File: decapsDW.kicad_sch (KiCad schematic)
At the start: 5 parts

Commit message: adding connectors for display and pi power, pin headers
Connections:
- net DW_VDD1 renamed 3V3_RADAR
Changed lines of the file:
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@@
-    (stroke (width 0) (type default))
-  )
-  (wire (pts (xy 22.86 43.18) (xy 22.86 27.94))
     (stroke (width 0) (type default))
   )
@@
     (stroke (width 0) (type default))
   )
-  (wire (pts (xy 22.86 43.18) (xy 29.21 43.18))
+  (wire (pts (xy 26.67 36.83) (xy 26.67 43.18))
+    (stroke (width 0) (type default))
+  )
+  (wire (pts (xy 26.67 43.18) (xy 29.21 43.18))
     (stroke (width 0) (type default))
   )
@@
     )
   )
-  (global_label "VOUT1" (shape bidirectional) (at 22.86 43.18 180) (fields_autoplaced)
-    (effects (font (size 1.27 1.27)) (justify right))
-    (property "Intersheetrefs" "${INTERSHEET_REFS}" (at 12.8368 43.18 0)
-      (effects (font (size 1.27 1.27)) (justify right) hide)
-    )
-  )
   (global_label "DW_VDD2B" (shape bidirectional) (at 62.23 82.55 0) (fields_autoplaced)
     (effects (font (size 1.27 1.27)) (justify left))
@@
     )
   )
+  (global_label "3V3_RADAR" (shape bidirectional) (at 26.67 43.18 180) (fields_autoplaced)
+    (effects (font (size 1.27 1.27)) (justify right))
+    (property "Intersheetrefs" "${INTERSHEET_REFS}" (at 12.1111 43.18 0)
+      (effects (font (size 1.27 1.27)) (justify right) hide)
+    )
+  )
   (global_label "DW_VDD1" (shape bidirectional) (at 60.96 43.18 0) (fields_autoplaced)
     (effects (font (size 1.27 1.27)) (justify left))
@@
     )
   )
-  (symbol (lib_id "power:PWR_FLAG") (at 22.86 27.94 0) (unit 1)
-    (in_bom yes) (on_board yes) (dnp no) (fields_autoplaced)
-    (property "Reference" "#FLG02" (at 22.86 26.035 0)
-      (effects (font (size 1.27 1.27)) hide)
-    )
-    (property "Value" "PWR_FLAG" (at 22.86 22.86 0)
-      (effects (font (size 1.27 1.27)))
-    )
-    (property "Footprint" "" (at 22.86 27.94 0)
-      (effects (font (size 1.27 1.27)) hide)
-    )
-    (property "Datasheet" "~" (at 22.86 27.94 0)
-      (effects (font (size 1.27 1.27)) hide)
-    )
+  (symbol (lib_id "power:PWR_FLAG") (at 26.67 36.83 0) (unit 1)
+    (in_bom yes) (on_board yes) (dnp no) (fields_autoplaced)
+    (property "Reference" "#FLG02" (at 26.67 34.925 0)
+      (effects (font (size 1.27 1.27)) hide)
+    )
+    (property "Value" "PWR_FLAG" (at 26.67 31.75 0)
+      (effects (font (size 1.27 1.27)))
+    )
+    (property "Footprint" "" (at 26.67 36.83 0)
+      (effects (font (size 1.27 1.27)) hide)
+    )
+    (property "Datasheet" "~" (at 26.67 36.83 0)
+      (effects (font (size 1.27 1.27)) hide)
+    )

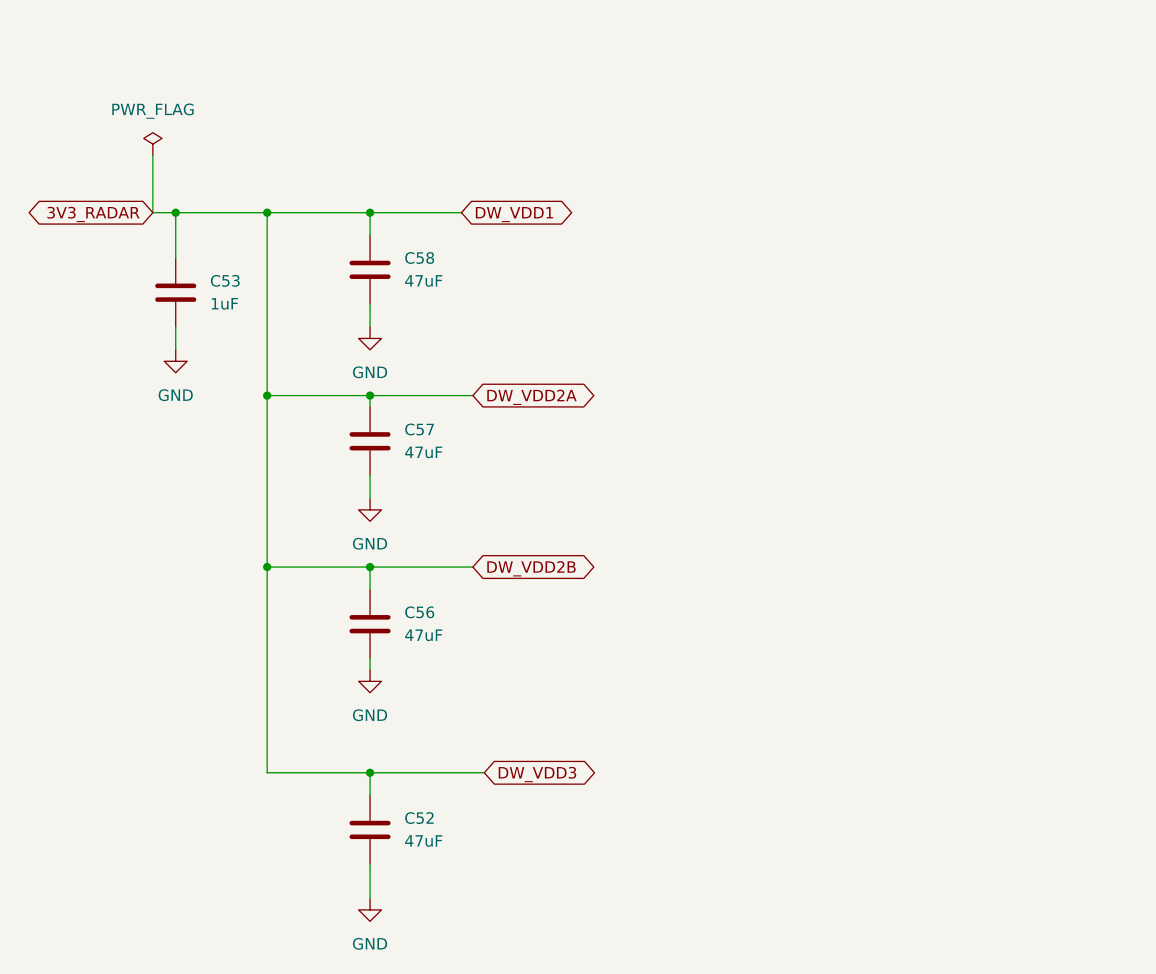
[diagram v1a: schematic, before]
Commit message: changing decoup cap sizes for rf ic
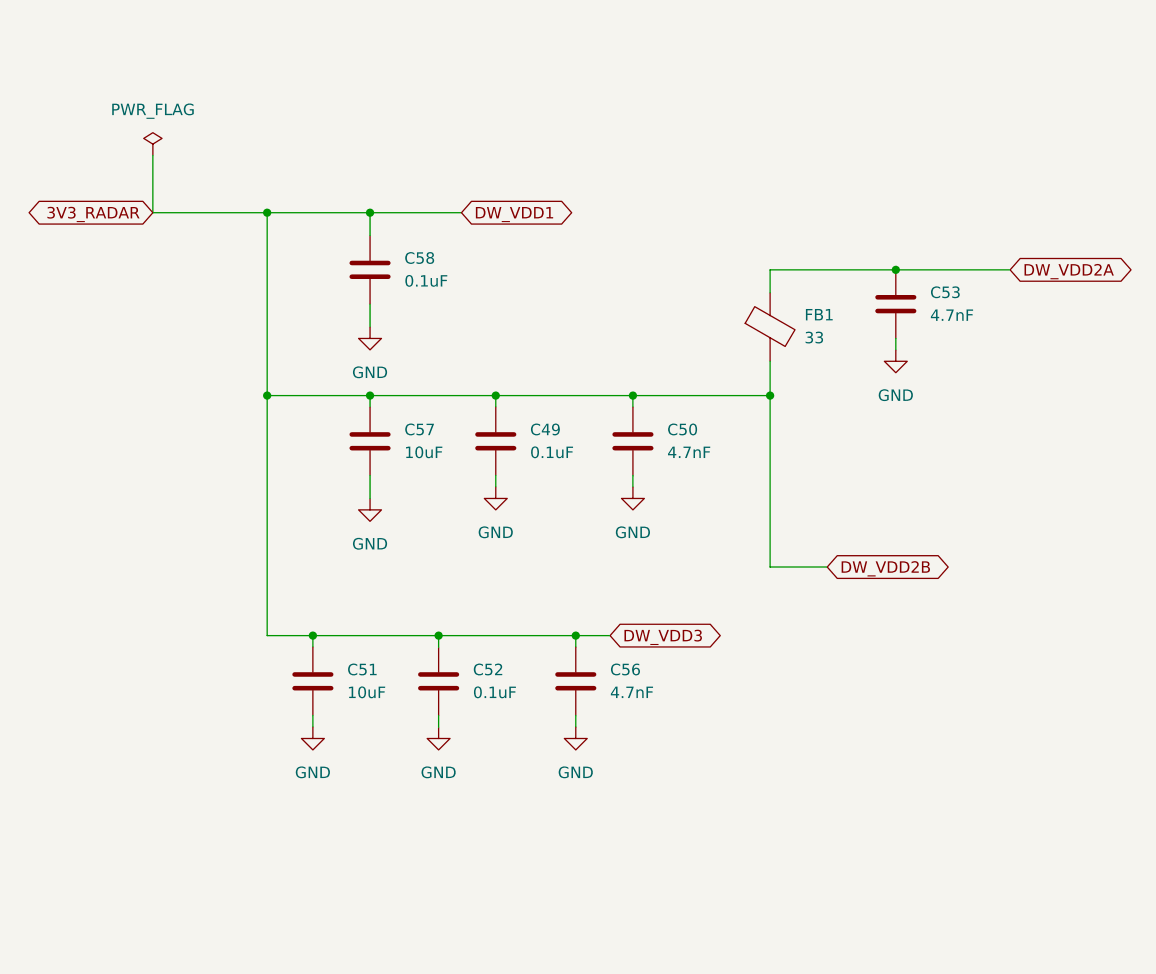
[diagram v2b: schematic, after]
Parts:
- added C49: 0.1uF, Capacitor_SMD:C_0402_1005Metric, symbol Device:C
- added C50: 4.7nF, Capacitor_SMD:C_0402_1005Metric, symbol Device:C
- added C51: 10uF, Capacitor_SMD:C_0402_1005Metric, symbol Device:C
- added FB1: 33, Capacitor_SMD:C_0402_1005Metric, symbol Device:FerriteBead
- C52, C58: value 47uF -> 0.1uF; footprint Capacitor_SMD:C_0603_1608Metric -> Capacitor_SMD:C_0402_1005Metric
- C53: value 1uF -> 4.7nF; footprint Capacitor_SMD:C_0603_1608Metric -> Capacitor_SMD:C_0402_1005Metric
- C56: value 47uF -> 4.7nF; footprint Capacitor_SMD:C_0603_1608Metric -> Capacitor_SMD:C_0402_1005Metric
- C57: value 47uF -> 10uF; footprint Capacitor_SMD:C_0603_1608Metric -> Capacitor_SMD:C_0402_1005Metric
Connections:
- net 3V3_RADAR: now also C49.1, C50.1, C51.1, FB1.2; no longer C53.1
- net GND: now also C49.2, C50.2, C51.2
- new net DW_VDD2A: C53.1, FB1.1
